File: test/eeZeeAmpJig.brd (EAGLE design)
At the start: 30.5 x 18.3 mm, 19 parts

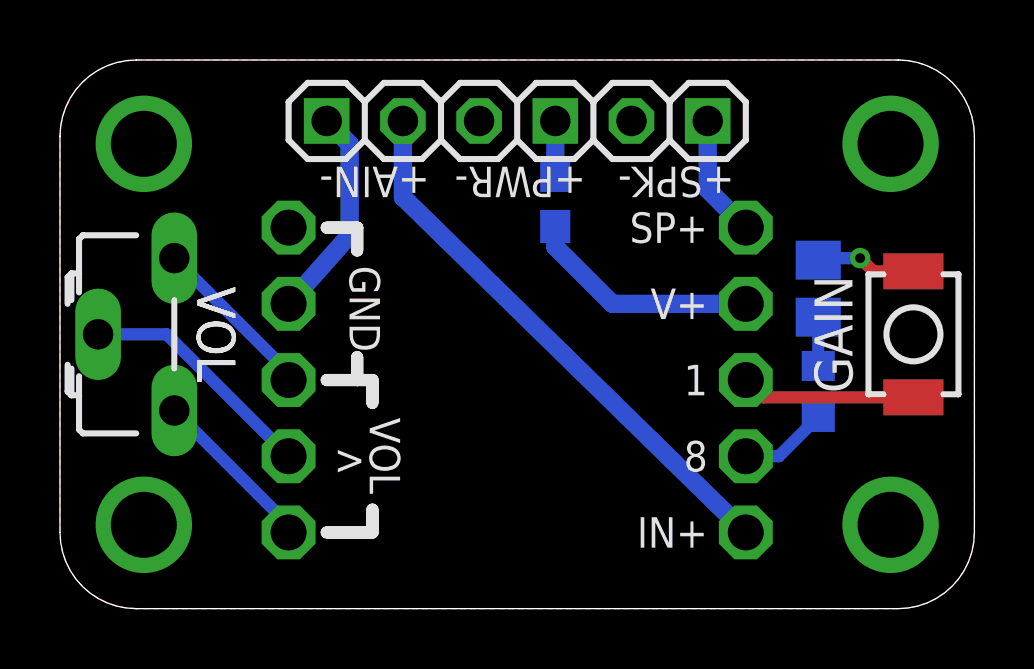
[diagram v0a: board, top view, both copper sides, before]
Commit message: added pogo pins for output audio cap
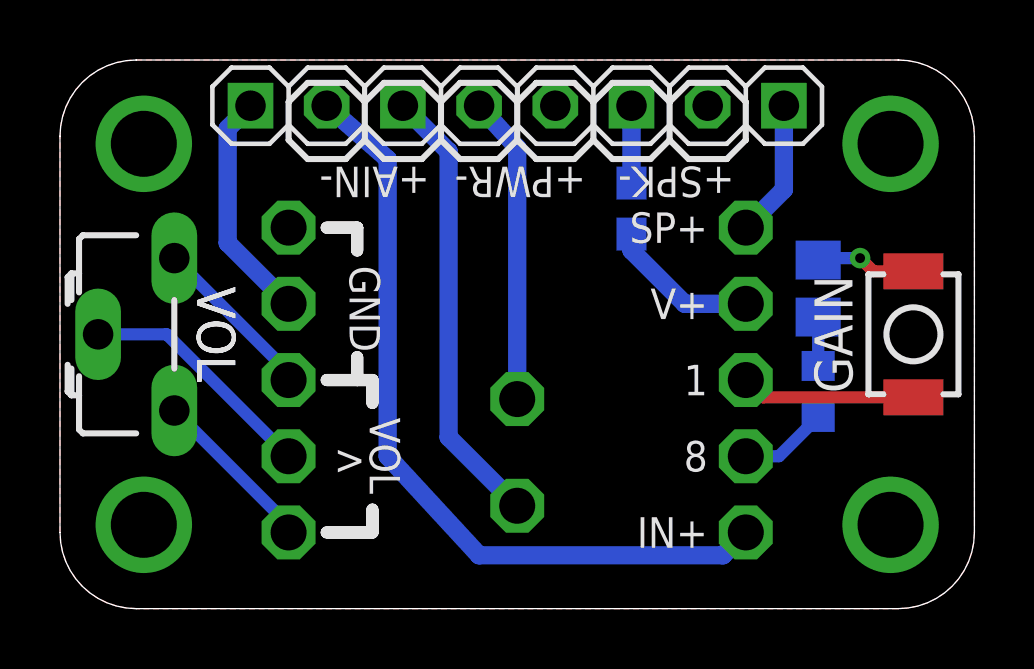
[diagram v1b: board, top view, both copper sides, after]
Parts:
- added JP2: +CAP-, pinhead-2:1X02-S
- added PAD6: CAP+, bt_electromech:POGO_1.02MM
- added PAD7: CAP-, bt_electromech:POGO_1.02MM
- moved JP1 2.59 mm to (17.8, 16.8)
- moved JP15 2.59 mm to (7.62, 16.8)
- moved JP14 2.59 mm to (22.9, 16.8)
- moved F1 2.55 mm to (19.1, 13.3)
- moved LOGO2 2.29 mm to (15.2, 12.6)
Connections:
- new net N$2: JP2.1, PAD6.P$1
- new net N$6: JP2.2, PAD7.P$1
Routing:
- net N$2: track 0.00 -> 14.9 mm
- net N$6: track 0.00 -> 10.3 mm
- net IN+: track 18.5 -> 26.3 mm
- net N$4: track 7.81 -> 5.09 mm
- net VCC: track 1.82 -> 2.58 mm
- net IN-: track 7.18 -> 7.76 mm
- net SPEAKER: track 4.08 -> 4.59 mm
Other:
- board text added: "R0.4"

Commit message: Fixed capacitor labels, polarity
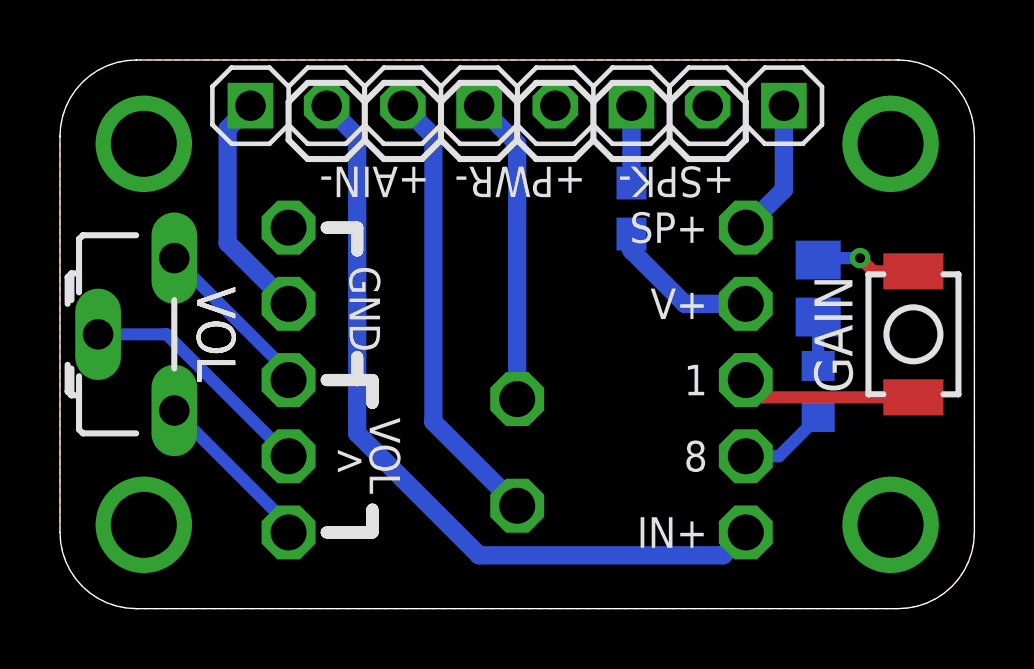
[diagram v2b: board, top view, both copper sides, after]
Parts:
- moved PAD6 3.56 mm to (15.2, 6.99), turned to 180 degrees
- moved PAD7 3.56 mm to (15.2, 3.43)
- turned JP2 to 180 degrees
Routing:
- net N$6: track 10.3 -> 14.9 mm
- net N$2: track 14.9 -> 10.3 mm
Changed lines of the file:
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@@
 <attribute name="VALUE" x="20.066" y="15.24" size="1.016" layer="27" font="vector" ratio="12" rot="SR180"/>
 </element>
-<element name="PAD6" library="bt_electromech" package="POGO_1.02MM" value="CAP+" x="15.24" y="3.429" smashed="yes">
+<element name="PAD6" library="bt_electromech" package="POGO_1.02MM" value="CAP+" x="15.24" y="6.985" smashed="yes" rot="R180">
+<attribute name="VALUE" x="13.97" y="8.255" size="1.016" layer="27" font="vector"/>
+</element>
+<element name="PAD7" library="bt_electromech" package="POGO_1.02MM" value="CAP-" x="15.24" y="3.429" smashed="yes">
 <attribute name="VALUE" x="13.97" y="1.143" size="1.016" layer="27" font="vector"/>
 </element>
-<element name="PAD7" library="bt_electromech" package="POGO_1.02MM" value="CAP-" x="15.24" y="6.985" smashed="yes">
-<attribute name="VALUE" x="13.97" y="8.255" size="1.016" layer="27" font="vector"/>
-</element>
-<element name="JP2" library="pinhead-2" package="1X02-S" value="+CAP-" x="12.7" y="16.764" smashed="yes">
+<element name="JP2" library="pinhead-2" package="1X02-S" value="+CAP-" x="12.7" y="16.764" smashed="yes" rot="R180">
 <attribute name="VALUE" x="14.986" y="15.24" size="1.016" layer="27" font="vector" ratio="12" rot="SR180"/>
 </element>
@@
 <contactref element="JP15" pad="2"/>
 <contactref element="PAD12" pad="P$1"/>
-<wire x1="8.89" y1="16.764" x2="10.922" y2="14.986" width="0.6096" layer="16"/>
-<wire x1="10.922" y1="14.986" x2="10.922" y2="5.08" width="0.6096" layer="16"/>
-<wire x1="10.922" y1="5.08" x2="13.97" y2="1.778" width="0.6096" layer="16"/>
+<wire x1="8.89" y1="16.764" x2="9.906" y2="15.748" width="0.6096" layer="16"/>
+<wire x1="9.906" y1="15.748" x2="9.906" y2="5.842" width="0.6096" layer="16"/>
+<wire x1="9.906" y1="5.842" x2="13.97" y2="1.778" width="0.6096" layer="16"/>
 <wire x1="13.97" y1="1.778" x2="22.098" y2="1.778" width="0.6096" layer="16"/>
 <wire x1="22.098" y1="1.778" x2="22.86" y2="2.54" width="0.6096" layer="16"/>
@@
 <contactref element="JP2" pad="1"/>
 <contactref element="PAD6" pad="P$1"/>
-<wire x1="11.43" y1="16.764" x2="12.954" y2="15.24" width="0.6096" layer="16"/>
-<wire x1="12.954" y1="15.24" x2="12.954" y2="5.715" width="0.6096" layer="16"/>
-<wire x1="12.954" y1="5.715" x2="15.24" y2="3.429" width="0.6096" layer="16"/>
+<wire x1="13.97" y1="16.764" x2="15.24" y2="15.494" width="0.6096" layer="16"/>
+<wire x1="15.24" y1="15.494" x2="15.24" y2="6.985" width="0.6096" layer="16"/>
 </signal>
 <signal name="N$6">
 <contactref element="JP2" pad="2"/>
 <contactref element="PAD7" pad="P$1"/>
-<wire x1="13.97" y1="16.764" x2="15.24" y2="15.367" width="0.6096" layer="16"/>
-<wire x1="15.24" y1="15.367" x2="15.24" y2="6.985" width="0.6096" layer="16"/>
+<wire x1="11.43" y1="16.764" x2="12.446" y2="15.748" width="0.6096" layer="16"/>
+<wire x1="12.446" y1="15.748" x2="12.446" y2="6.223" width="0.6096" layer="16"/>
+<wire x1="15.24" y1="3.429" x2="12.446" y2="6.223" width="0.6096" layer="16"/>
 </signal>
 </signals>
